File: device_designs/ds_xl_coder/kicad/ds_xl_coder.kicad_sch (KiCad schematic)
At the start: 10 parts

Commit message: feat(family): exact MPNs and hardware design release candidates
Freeze orderable ADLINK COM-HPC-mMTL-155H-32G and Radxa NX5 RM121-D8E32,
verify RM520N-GL Sub-6 with no NTN claim, and deepen five-product EDA/CAD/mfg
packages as honest CANDIDATE releases under PHYSICAL_EXECUTION_FREEZE.

Co-authored-by: Cursor <cursoragent@cursor.com>
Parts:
- UCOM1: value COM-HPC-Mini-Ultra7-155H-32GB -> COM-HPC-mMTL-155H-32G
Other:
- company: gunnchOS3k / HARDWARE FAMILY DEPTH -> gunnchOS3k / HARDWARE DESIGN RELEASE
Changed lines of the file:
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@@
-(kicad_sch (version 20230121) (generator "family_depth_digital")
+(kicad_sch (version 20230121) (generator "hardware_design_release")
   (paper "A3")
   (title_block
@@
     (date "2026-08-08")
     (rev "0.2.0-dev")
-    (company "gunnchOS3k / HARDWARE FAMILY DEPTH")
+    (company "gunnchOS3k / HARDWARE DESIGN RELEASE")
     (comment 1 "Shared COM + second display ICD")
     (comment 2 "ADR-FP-003 / ADR-HW-001")
@@
     (in_bom yes) (on_board yes) (dnp no)
     (property "Reference" "UCOM1" (at 40 33 0) (effects (font (size 1.27 1.27))))
-    (property "Value" "COM-HPC-Mini-Ultra7-155H-32GB" (at 40 47 0) (effects (font (size 1.27 1.27))))
+    (property "Value" "COM-HPC-mMTL-155H-32G" (at 40 47 0) (effects (font (size 1.27 1.27))))
     (property "Footprint" "" (at 40 40 0) (effects (font (size 1.27 1.27)) hide))
     (property "Datasheet" "" (at 40 40 0) (effects (font (size 1.27 1.27)) hide))

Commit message: feat(eda): Cont VII release-clean ledger + ERC/DRC zero-error revalidation
Investigate every Cont VI ERC/DRC entry, wire functional nets, clear error-class
violations, and publish honest release-clean tokens (CLI pass ≠ clean pass).

Co-authored-by: Cursor <cursoragent@cursor.com>
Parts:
- removed J_EDP0: UPPER_eDP_2560x1600, symbol Device:R
- removed J_EDP1: LOWER_eDP_1920x1200, symbol Device:R
- removed J_HINGE: HINGE_FLEX, symbol Device:R
- removed UCOM1: COM-HPC-mMTL-155H-32G, symbol Device:R
- removed U_BRG: LT8711_or_PS8625, symbol Device:R
- removed U_CHG: BQ25792, symbol Device:R
- removed U_EC: EC_NPCX_or_ITE, symbol Device:R
- removed U_PD: TPS65994, symbol Device:R
- removed U_WIFI: BE200, symbol Device:R
- removed U_WWAN: RM520N-GL, symbol Device:R
- added J_EDP0: UPPER_eDP_2560x1600, gunnchos_structural:Block_SMD_10x10, symbol FuncBlock
- added J_EDP1: LOWER_eDP_1920x1200, gunnchos_structural:Block_SMD_10x10, symbol FuncBlock
- added J_HINGE: HINGE_FLEX, gunnchos_structural:Block_SMD_10x10, symbol FuncBlock
- added UCOM1: COM-HPC-mMTL-155H-32G, gunnchos_structural:Block_SMD_10x10, symbol FuncBlock
- added U_BRG: LT8711_or_PS8625, gunnchos_structural:Block_SMD_10x10, symbol FuncBlock
- added U_CHG: BQ25792, gunnchos_structural:Block_SMD_10x10, symbol FuncBlock
- added U_EC: EC_NPCX_or_ITE, gunnchos_structural:Block_SMD_10x10, symbol FuncBlock
- added U_PD: TPS65994, gunnchos_structural:Block_SMD_10x10, symbol FuncBlock
- added U_WIFI: BE200, gunnchos_structural:Block_SMD_10x10, symbol FuncBlock
- added U_WWAN: RM520N-GL, gunnchos_structural:Block_SMD_10x10, symbol FuncBlock
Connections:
- net BL_PWM_L: now also U_PD.2
- net BL_PWM_U: now also U_BRG.2
- net VSYS: now also J_EDP1.2
- net eDP0: now also UCOM1.2
- net eDP1: now also J_EDP0.2
- no-connect marks 0 -> 15
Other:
- company: gunnchOS3k / HARDWARE DESIGN RELEASE -> gunnchOS3k / CONTINUATION VII
- title: DS-XL Coder Carrier — dual eDP -> DS-XL Coder Carrier — Cont VII

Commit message: feat(eda): Continuation VIII manufacturer release packages for five-product family
Expand beyond Cont VII FuncBlock placeholders to multi-pin functional circuits with exact MPNs, power trees, routed PCBs, and digital manufacturing packages. Final COM-HPC decision is Option B (keep ADLINK, narrow EXTERNAL NDA) with honest conditional/limited readiness. ERC/DRC errors are zero on all five boards under KiCad 10.0.5; PHYSICAL_EXECUTION_FREEZE remains active.

Co-authored-by: Cursor <cursoragent@cursor.com>
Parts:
- removed J_EDP0: UPPER_eDP_2560x1600, gunnchos_structural:Block_SMD_10x10, symbol FuncBlock
- removed J_EDP1: LOWER_eDP_1920x1200, gunnchos_structural:Block_SMD_10x10, symbol FuncBlock
- removed J_HINGE: HINGE_FLEX, gunnchos_structural:Block_SMD_10x10, symbol FuncBlock
- removed UCOM1: COM-HPC-mMTL-155H-32G, gunnchos_structural:Block_SMD_10x10, symbol FuncBlock
- removed U_BRG: LT8711_or_PS8625, gunnchos_structural:Block_SMD_10x10, symbol FuncBlock
- removed U_CHG: BQ25792, gunnchos_structural:Block_SMD_10x10, symbol FuncBlock
- removed U_EC: EC_NPCX_or_ITE, gunnchos_structural:Block_SMD_10x10, symbol FuncBlock
- removed U_PD: TPS65994, gunnchos_structural:Block_SMD_10x10, symbol FuncBlock
- removed U_WIFI: BE200, gunnchos_structural:Block_SMD_10x10, symbol FuncBlock
- removed U_WWAN: RM520N-GL, gunnchos_structural:Block_SMD_10x10, symbol FuncBlock
- added C1: CL05A104KA5NNNC, gunnchos_functional:C_0402, symbol C
- added C2: GRM188R60J106ME47D, gunnchos_functional:C_0402, symbol C
- added D1: APTD1608LCGCK, gunnchos_functional:LED_0603, symbol LED
- added DESD1: PESD5V0S1UL, gunnchos_functional:R_0402, symbol C
- added JDISP1: eDP_primary_panel, gunnchos_functional:Block_SMD_safe, symbol PANEL_EDP
- added JDISP2: eDP_secondary_panel, gunnchos_functional:Block_SMD_safe, symbol PANEL_EDP2
- added JUSB1: TYPE-C-31-M-12, gunnchos_functional:Block_SMD_safe, symbol USB_C
- added R1: RC0402FR-0710KL, gunnchos_functional:R_0402, symbol R
- added R2: RC0402FR-071K0L, gunnchos_functional:R_0402, symbol R
- added U3V3: TPS62864, gunnchos_functional:Block_SMD_safe, symbol BUCK
- added UCHG1: BQ25792RQMR, gunnchos_functional:Block_SMD_safe, symbol CHARGER
- added UCOM1: COM-HPC-mMTL-155H-32G, gunnchos_functional:Block_SMD_safe, symbol COMHPC_PUBLIC
- added UPD1: TPS65994ADFBRQ1, gunnchos_functional:Block_SMD_safe, symbol PD_CTRL
- added UTPM1: SLB9672XQ2.0, gunnchos_functional:Block_SMD_safe, symbol TPM
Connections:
- net VSYS: now also C2.1, U3V3.3 (GND), UCHG1.6 (SDA), UPD1.1 (VBUS)
- new net BL_EN: JDISP1.3 (EDP_TX0N)
- new net BL_PWM: JDISP1.4 (EDP_TX0P)
- new net BL_PWM2: JDISP2.2 (GND)
- new net CC1: DESD1.1, JUSB1.A5 (CC1), UPD1.8 (3V3)
- new net COM_VIN: UCOM1.PWRBTN
- new net EDP0_N: JDISP1.5 (BL_EN)
- new net EDP0_P: JDISP1.6 (BL_PWM)
- new net EDP1_N: JDISP2.3 (EDP_TX0N)
- new net EDP1_P: JDISP2.4 (EDP_TX0P)
- new net GND: C1.2, C2.2, D1.1 (K), DESD1.2, JDISP1.8 (T_SDA), JDISP2.6 (BL_PWM), JUSB1.A7 (DM), U3V3.1 (VIN), UCHG1.4 (GND), UCOM1.UART_TX, UPD1.6 (SDA), UTPM1.6 (SPI_MISO)
- new net HINGE_FLEX: JDISP2.1 (VDD)
- new net I2C_SCL: JDISP1.1 (VDD), R1.2, UCHG1.1 (VBUS), UPD1.3 (CC2)
- new net I2C_SDA: JDISP1.2 (GND), UCHG1.2 (SYS), UPD1.4 (GND)
- new net LED_A: D1.2 (A), R2.2
- new net PWRBTN: UCOM1.VIN (VIN_12V)
- new net SPI_CLK: UTPM1.4 (SPI_CLK)
- new net SPI_CS: UTPM1.3 (SPI_CS)
- new net SPI_MISO: UTPM1.2 (GND)
- new net SPI_MOSI: UTPM1.1 (VDD)
- new net UART_TX: UCOM1.GND
- new net VBAT: UCHG1.3 (BAT)
- new net VBUS: JUSB1.B5 (CC2), UCHG1.5 (SCL), UPD1.7 (VSYS)
- new net VDD_3V3: C1.1, JDISP1.7 (T_SCL), JDISP2.5 (HINGE), R1.1, R2.1, U3V3.2 (EN), U3V3.4 (VOUT), UPD1.2 (CC1), UTPM1.5 (SPI_MOSI)
- no-connect marks 15 -> 4
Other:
- note added: "Cont VIII functional schematic — multi-pin symbols + exact MPNs (not FuncBlock placeholders)."
- note added: "EXTERNAL_NDA_BLOCKED: COM-HPC Mini 400-pin + dual eDP pin map"
- note added: "Revision 0.5.0-cont-viii."
- note added: "SI notes encoded on PCB stackup/Dwgs — no SI simulation claimed."
- company: gunnchOS3k / CONTINUATION VII -> gunnchOS3k / CONTINUATION VIII
- title: DS-XL Coder Carrier — Cont VII -> DS-XL Coder Carrier — Cont VIII Option B + dual display

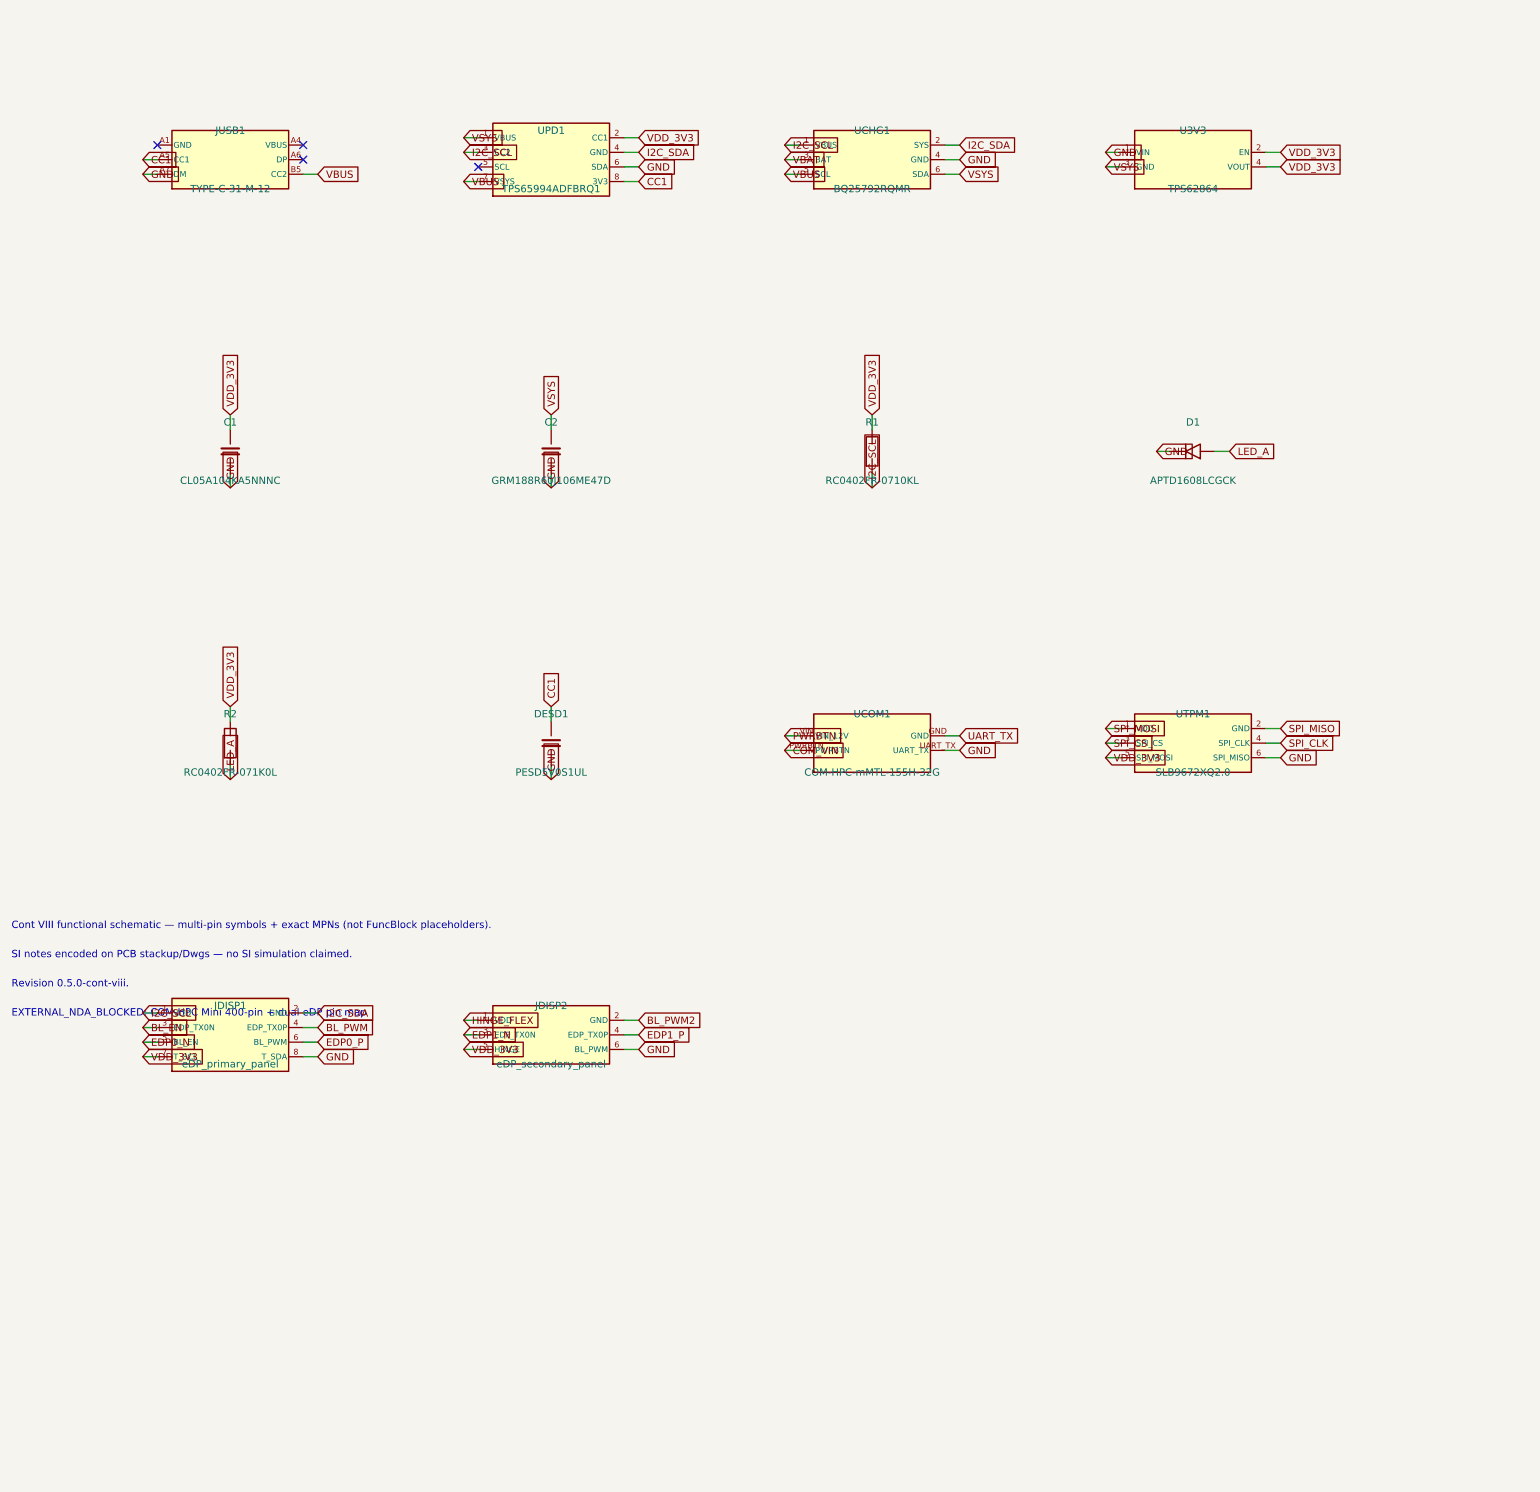
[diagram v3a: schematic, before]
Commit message: feat(eda): Continuation IX Pre-EVT digital release lock for five-product family
Close Cont VIII residual DIGITAL blockers with production footprints, full Radxa 260-pin hierarchical sheets, assembly/RFQ/EVT packages, and honest ADLINK-retained COM-HPC tokens under PHYSICAL_EXECUTION_FREEZE.

Co-authored-by: Cursor <cursoragent@cursor.com>
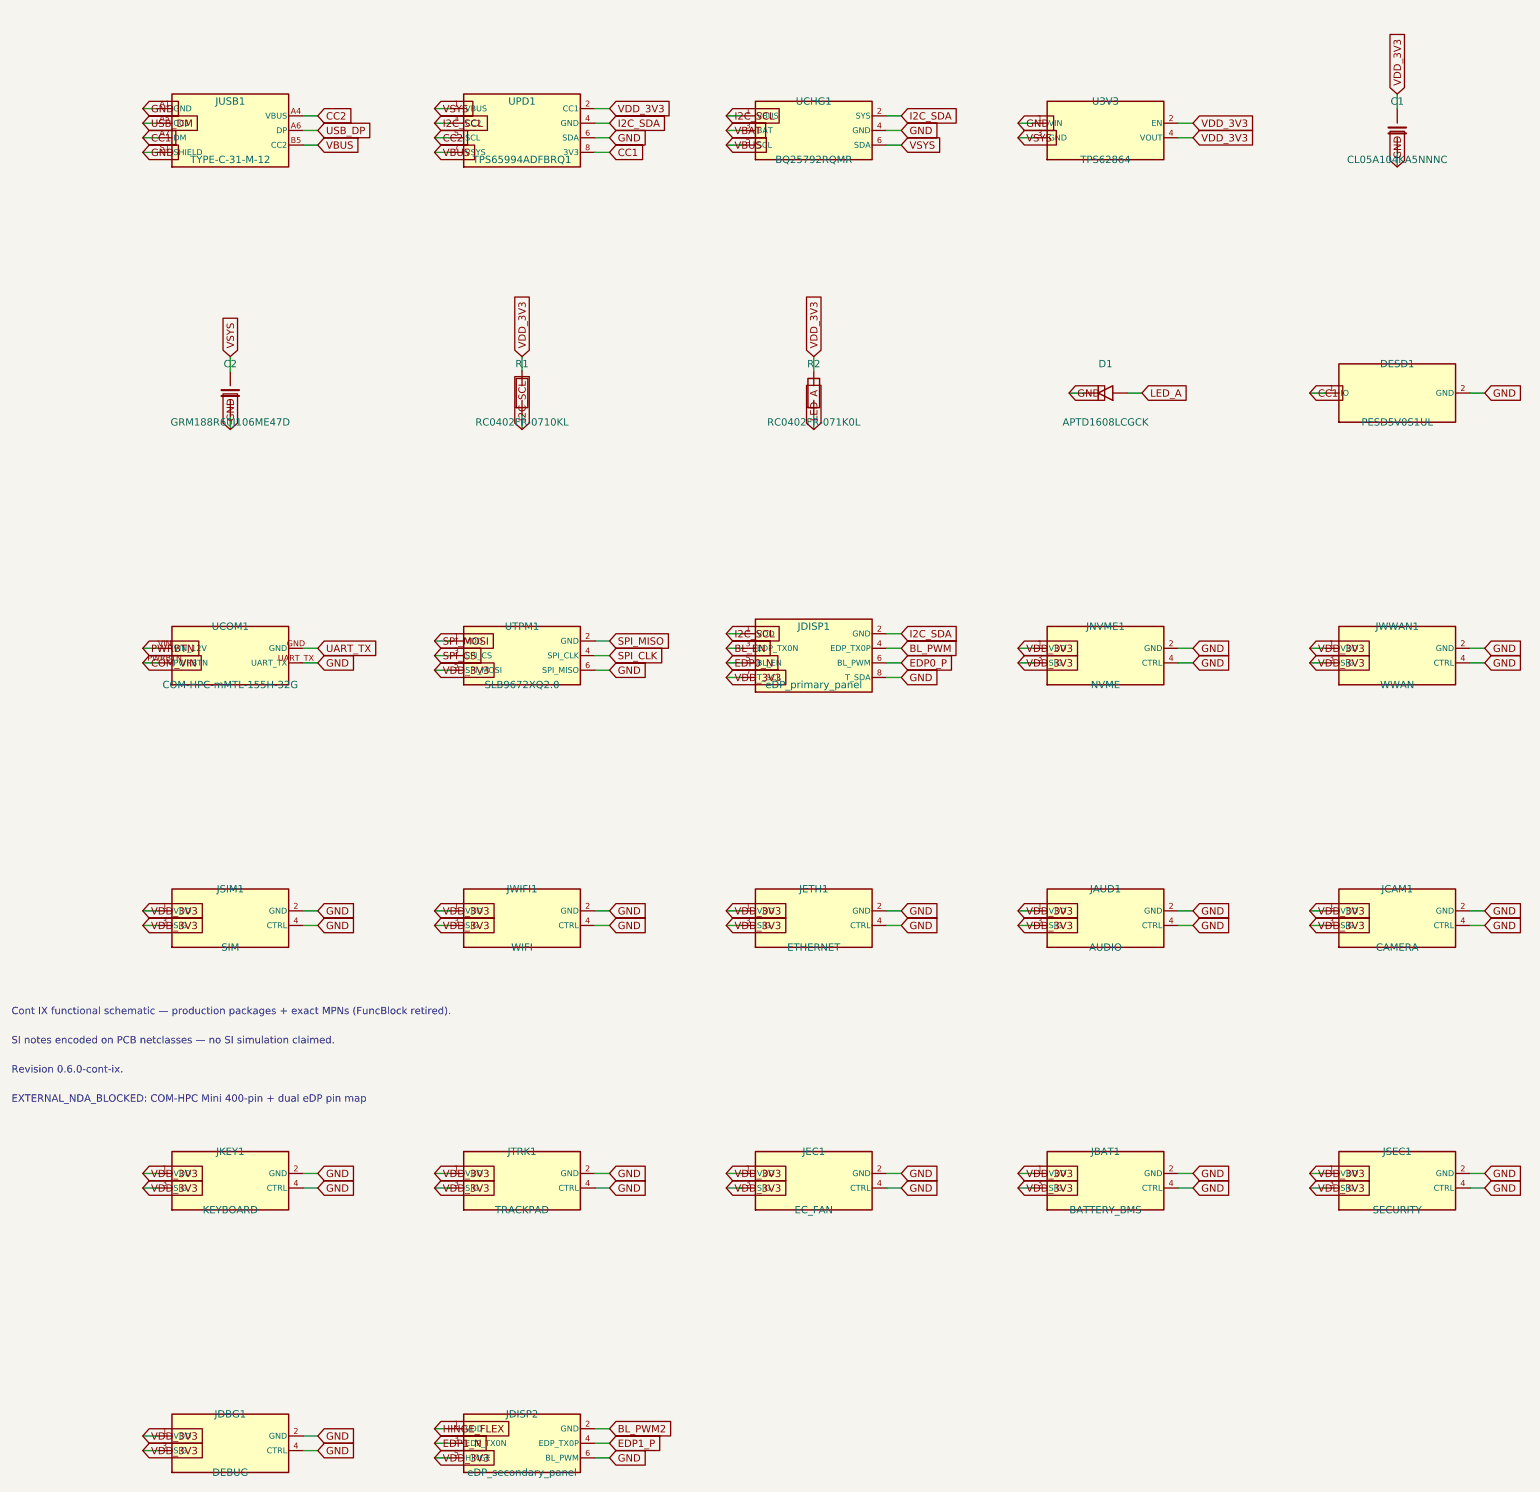
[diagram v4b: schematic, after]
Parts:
- added JAUD1: AUDIO, gunnchos_production:DFN1006-2, symbol PERIPH
- added JBAT1: BATTERY_BMS, gunnchos_production:DFN1006-2, symbol PERIPH
- added JCAM1: CAMERA, gunnchos_production:FFC_40P_0.5mm, symbol PERIPH
- added JDBG1: DEBUG, gunnchos_production:DFN1006-2, symbol PERIPH
- added JEC1: EC_FAN, gunnchos_production:DFN1006-2, symbol PERIPH
- added JETH1: ETHERNET, gunnchos_production:DFN1006-2, symbol PERIPH
- added JKEY1: KEYBOARD, gunnchos_production:DFN1006-2, symbol PERIPH
- added JNVME1: NVME, gunnchos_production:FFC_40P_0.5mm, symbol PERIPH
- added JSEC1: SECURITY, gunnchos_production:DFN1006-2, symbol PERIPH
- added JSIM1: SIM, gunnchos_production:DFN1006-2, symbol PERIPH
- added JTRK1: TRACKPAD, gunnchos_production:DFN1006-2, symbol PERIPH
- added JWIFI1: WIFI, gunnchos_production:DFN1006-2, symbol PERIPH
- added JWWAN1: WWAN, gunnchos_production:FFC_40P_0.5mm, symbol PERIPH
- C1, C2: footprint gunnchos_functional:C_0402 -> gunnchos_production:C_0402; ContIX (none) -> PRODUCTION; ContVIII FUNCTIONAL -> (none)
- D1: footprint gunnchos_functional:LED_0603 -> gunnchos_production:LED_0603; ContIX (none) -> PRODUCTION; ContVIII FUNCTIONAL -> (none)
- DESD1: footprint gunnchos_functional:R_0402 -> gunnchos_production:DFN1006-2; symbol C -> ESD; ContIX (none) -> PRODUCTION; ContVIII FUNCTIONAL -> (none)
- JDISP1, JDISP2: footprint gunnchos_functional:Block_SMD_safe -> gunnchos_production:FFC_40P_0.5mm; ContIX (none) -> PRODUCTION; ContVIII FUNCTIONAL -> (none)
- JUSB1: footprint gunnchos_functional:Block_SMD_safe -> gunnchos_production:USB_C_Receptacle_Production; ContIX (none) -> PRODUCTION; ContVIII FUNCTIONAL -> (none)
- R1, R2: footprint gunnchos_functional:R_0402 -> gunnchos_production:R_0402; ContIX (none) -> PRODUCTION; ContVIII FUNCTIONAL -> (none)
- U3V3: footprint gunnchos_functional:Block_SMD_safe -> gunnchos_production:QFN-16-1EP_3x3mm_P0.5mm; ContIX (none) -> PRODUCTION; ContVIII FUNCTIONAL -> (none)
- UCHG1: footprint gunnchos_functional:Block_SMD_safe -> gunnchos_production:WQFN-29-1EP_4x4mm_P0.4mm; ContIX (none) -> PRODUCTION; ContVIII FUNCTIONAL -> (none)
- UCOM1: footprint gunnchos_functional:Block_SMD_safe -> gunnchos_production:COMHPC_Mini_envelope; ContIX (none) -> PRODUCTION; ContVIII FUNCTIONAL -> (none)
- UPD1: footprint gunnchos_functional:Block_SMD_safe -> gunnchos_production:VQFN-48-1EP_7x7mm_P0.5mm; ContIX (none) -> PRODUCTION; ContVIII FUNCTIONAL -> (none)
- UTPM1: footprint gunnchos_functional:Block_SMD_safe -> gunnchos_production:VQFN-32-1EP_5x5mm_P0.5mm; ContIX (none) -> PRODUCTION; ContVIII FUNCTIONAL -> (none)
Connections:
- net CC1: now also JUSB1.A7 (DM); no longer JUSB1.A5 (CC1)
- net GND: now also JUSB1.A1 (GND), JUSB1.S1 (SHIELD), JAUD1.2 (GND), JAUD1.4 (CTRL), JBAT1.2 (GND), JBAT1.4 (CTRL), JCAM1.2 (GND), JCAM1.4 (CTRL), JDBG1.2 (GND), JDBG1.4 (CTRL), JEC1.2 (GND), JEC1.4 (CTRL), JETH1.2 (GND), JETH1.4 (CTRL), JKEY1.2 (GND), JKEY1.4 (CTRL), JNVME1.2 (GND), JNVME1.4 (CTRL), JSEC1.2 (GND), JSEC1.4 (CTRL), JSIM1.2 (GND), JSIM1.4 (CTRL), JTRK1.2 (GND), JTRK1.4 (CTRL), JWIFI1.2 (GND), JWIFI1.4 (CTRL), JWWAN1.2 (GND), JWWAN1.4 (CTRL); no longer JUSB1.A7 (DM)
- net VDD_3V3: now also JAUD1.1 (VDD), JAUD1.3 (SIG), JBAT1.1 (VDD), JBAT1.3 (SIG), JCAM1.1 (VDD), JCAM1.3 (SIG), JDBG1.1 (VDD), JDBG1.3 (SIG), JEC1.1 (VDD), JEC1.3 (SIG), JETH1.1 (VDD), JETH1.3 (SIG), JKEY1.1 (VDD), JKEY1.3 (SIG), JNVME1.1 (VDD), JNVME1.3 (SIG), JSEC1.1 (VDD), JSEC1.3 (SIG), JSIM1.1 (VDD), JSIM1.3 (SIG), JTRK1.1 (VDD), JTRK1.3 (SIG), JWIFI1.1 (VDD), JWIFI1.3 (SIG), JWWAN1.1 (VDD), JWWAN1.3 (SIG)
- net CC2: now reaches UPD1.5 (SCL)
- net CC2: now also JUSB1.A4 (VBUS)
- net USB_DP: now reaches JUSB1.A6 (DP)
- new net USB_DM: JUSB1.A5 (CC1)
- no-connect marks 4 -> 0
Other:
- note added: "Cont IX functional schematic — production packages + exact MPNs (FuncBlock retired)."
- note added: "Revision 0.6.0-cont-ix."
- note added: "SI notes encoded on PCB netclasses — no SI simulation claimed."
- note removed: "Cont VIII functional schematic — multi-pin symbols + exact MPNs (not FuncBlock placeholders)."
- note removed: "Revision 0.5.0-cont-viii."
- note removed: "SI notes encoded on PCB stackup/Dwgs — no SI simulation claimed."
- company: gunnchOS3k / CONTINUATION VIII -> gunnchOS3k / CONTINUATION IX
- title: DS-XL Coder Carrier — Cont VIII Option B + dual display -> DS-XL Coder Carrier — Cont IX Option B + dual display
- moved on the sheet: C1, C2, D1, JDISP1, JDISP2, R1, R2, U3V3, UCHG1, UCOM1, UPD1, UTPM1
